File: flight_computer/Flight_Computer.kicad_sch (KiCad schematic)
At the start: 116 parts

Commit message: conn male+gnd
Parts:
- removed J? (x2): Conn_01x03_Male, symbol Connector:Conn_01x03_Male
- added J1, J2: Conn_01x02_Male, symbol Connector:Conn_01x02_Male
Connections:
- net +5V: now also J1.1 (Pin_1), J2.1 (Pin_1)
- net GND: now also J1.2 (Pin_2), J2.2 (Pin_2)

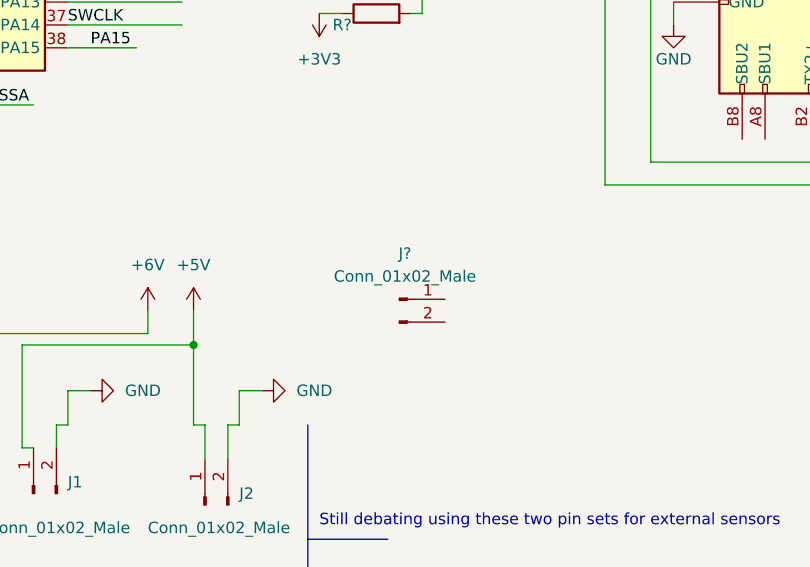
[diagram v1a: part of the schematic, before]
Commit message: conn male+gnd
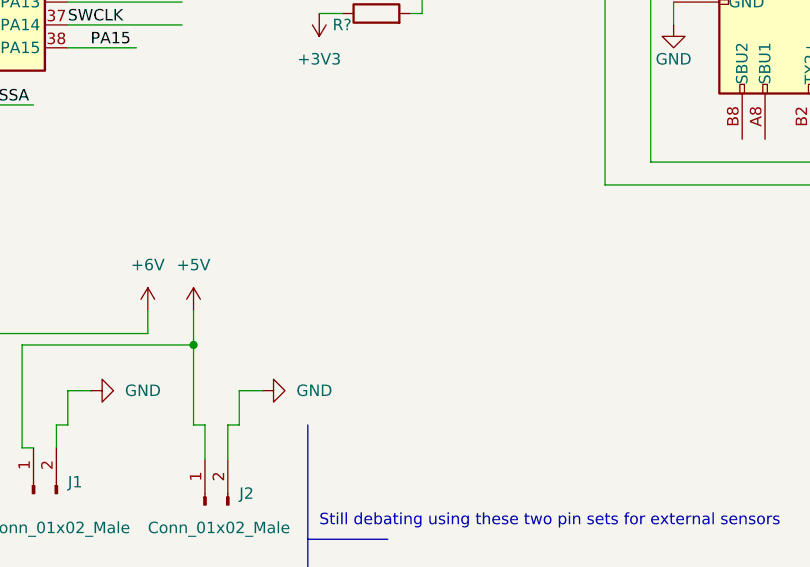
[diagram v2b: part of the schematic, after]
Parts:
- removed J?: Conn_01x02_Male, symbol Connector:Conn_01x02_Male
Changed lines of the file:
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@@
-    )
-  )
-  (symbol (lib_id "Connector:Conn_01x02_Male") (at 134.62 143.51 0) (unit 1)
-    (in_bom yes) (on_board yes) (dnp no) (fields_autoplaced)
-    (property "Reference" "J?" (at 135.255 138.43 0)
-      (effects (font (size 1.27 1.27)))
-    )
-    (property "Value" "Conn_01x02_Male" (at 135.255 140.97 0)
-      (effects (font (size 1.27 1.27)))
-    )
-    (property "Footprint" "" (at 134.62 143.51 0)
-      (effects (font (size 1.27 1.27)) hide)
-    )
-    (property "Datasheet" "~" (at 134.62 143.51 0)
-      (effects (font (size 1.27 1.27)) hide)
-    )
-    (pin "1")
-    (pin "2")
-    (instances
-      (project "Flight_Computer"
-        (path "/ac775286-301e-45e2-ba88-36489bae5295"
-          (reference "J?") (unit 1)
-        )
-      )
     )
   )
